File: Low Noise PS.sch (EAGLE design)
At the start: 64 parts, among them IC1 MAX6350SO08, IC2 OP27, IC3 LT1677, IC4 LT1677, IC5 MC79M12CDTG, IC6 MC78M12BDTG, Q1 MMBT2907AMMBTA56SOT23, Q2 MMBT5550SOT23, Q3 PMBF170, Q4 BSH201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

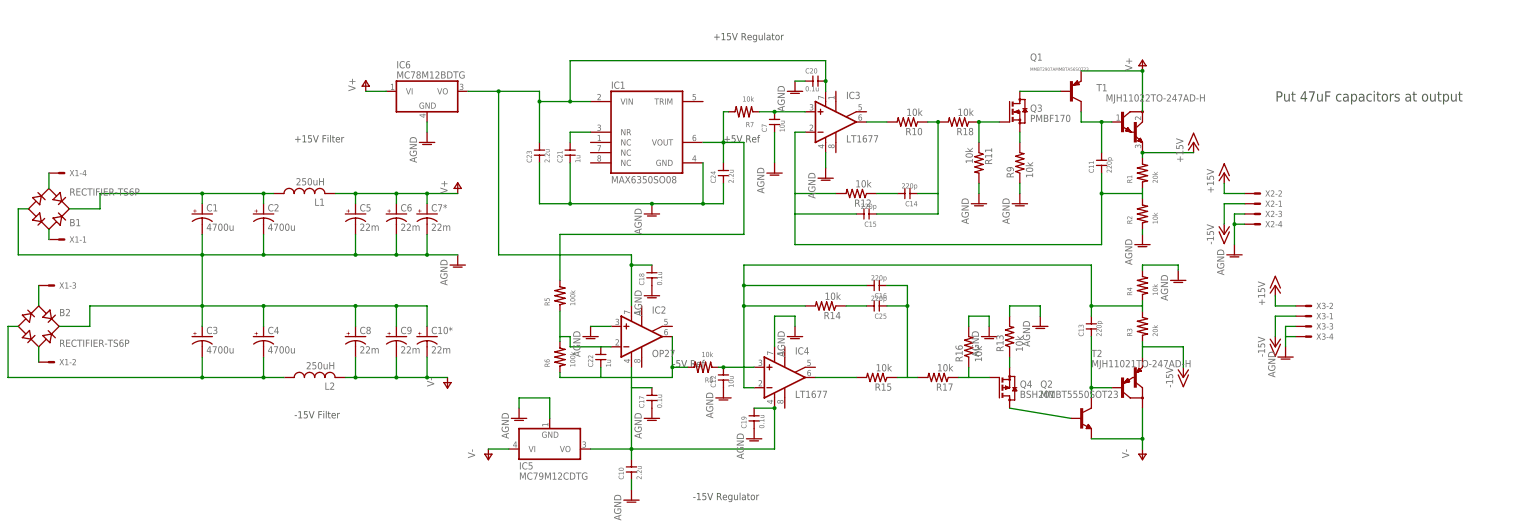
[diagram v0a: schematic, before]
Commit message: Almost ready to print
1) "cosmetic" adjustments needed (mainly increasing clearance for traces
below SMD parts)
2) component values need to be adjusted and chosen
3) Silkscreen needs to be cleaned
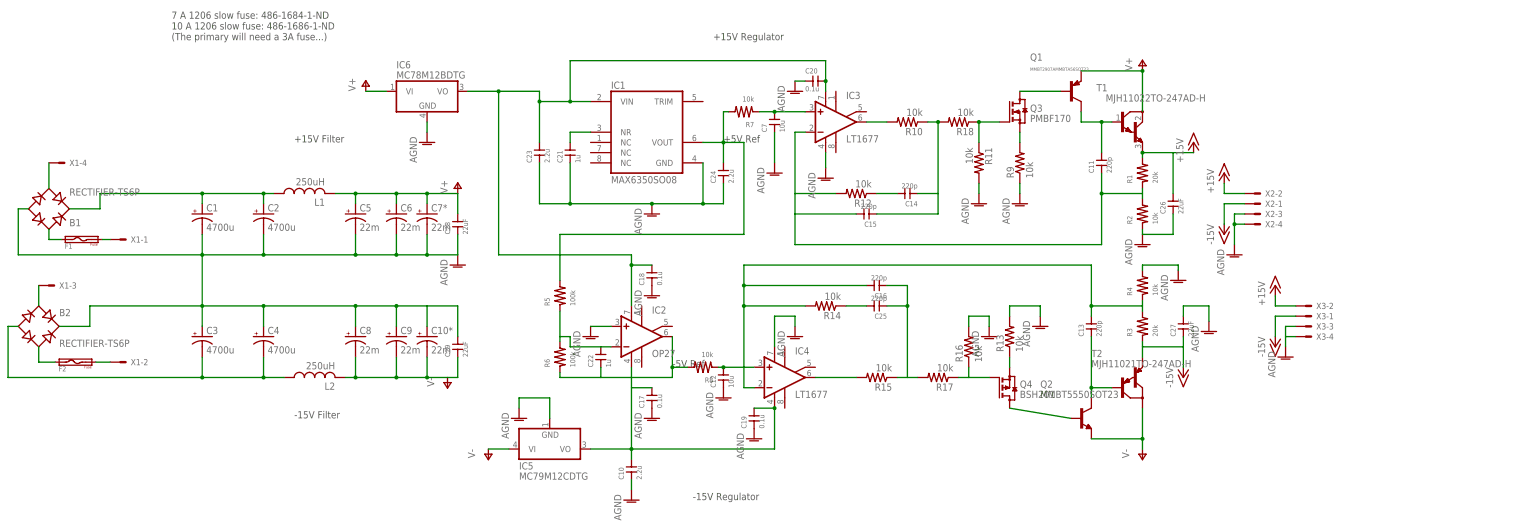
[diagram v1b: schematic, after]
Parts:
- added C26, C27, C28, C29: 22uF, rlc-jqi:CAP1206
- added F1, F2: (no value), jqi-power-supply:FUSE1206
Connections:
- new net N$22: F2.P$2, X1-2.S
- new net N$24: B2.AC2, F2.P$1
- net +15V: now also C26.P$2
- net -15V: now also C27.P$1
- net AGND: now also C26.P$1, C27.P$2, C28.P$1, C29.P$2
- net N$1: now also F1.P$1; no longer X1-1.S
- net N$5: now also F1.P$2, X1-1.S; no longer B2.AC2, X1-2.S
- net V+: now also C28.P$2
- net V-: now also C29.P$1
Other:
- note added: "7 A 1206 slow fuse: 486-1684-1-ND 10 A 1206 slow fuse: 486-1686-1-ND (The primary will need a 3A fuse...)"
- note removed: "Put 47uF capacitors at output"
- moved on the sheet: X1-1, X1-2, X1-4
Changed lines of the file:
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@@
 <part name="R17" library="rcl" deviceset="R-US_" device="R1206" value="10k"/>
 <part name="R18" library="rcl" deviceset="R-US_" device="R1206" value="10k"/>
+<part name="F1" library="jqi-power-supply" deviceset="FUSE" device="1206">
+<attribute name="DIGIKEY" value="486-1686-1-ND"/>
+</part>
+<part name="F2" library="jqi-power-supply" deviceset="FUSE" device="1206">
+<attribute name="DIGIKEY" value="486-1686-1-ND"/>
+</part>
+<part name="C26" library="rlc-jqi" deviceset="CAP" device="1206" value="22uF">
+<attribute name="DIGIKEY" value="445-8045-1-ND"/>
+</part>
+<part name="C27" library="rlc-jqi" deviceset="CAP" device="1206" value="22uF">
+<attribute name="DIGIKEY" value="445-8045-1-ND"/>
+</part>
+<part name="AGND23" library="supply1" deviceset="AGND" device=""/>
+<part name="C28" library="rlc-jqi" deviceset="CAP" device="1206" value="22uF">
+<attribute name="DIGIKEY" value="445-8045-1-ND"/>
+</part>
+<part name="C29" library="rlc-jqi" deviceset="CAP" device="1206" value="22uF">
+<attribute name="DIGIKEY" value="445-8045-1-ND"/>
+</part>
 </parts>
 <sheets>
@@
 <text x="190.5" y="2.54" size="1.778" layer="97">-15V Filter</text>
 <text x="190.5" y="71.12" size="1.778" layer="97">+15V Filter</text>
-<text x="434.34" y="81.28" size="2.54" layer="97">Put 47uF capacitors at output</text>
+<text x="160.02" y="96.52" size="1.778" layer="97">7 A 1206 slow fuse: 486-1684-1-ND
+10 A 1206 slow fuse: 486-1686-1-ND
+(The primary will need a 3A fuse...)</text>
 </plain>
 <instances>
-<instance part="X1" gate="-1" x="132.08" y="46.99"/>
-<instance part="X1" gate="-2" x="129.54" y="16.51"/>
+<instance part="X1" gate="-1" x="147.32" y="46.99"/>
+<instance part="X1" gate="-2" x="147.32" y="16.51"/>
 <instance part="X1" gate="-3" x="129.54" y="35.56"/>
-<instance part="X1" gate="-4" x="132.08" y="63.5"/>
+<instance part="X1" gate="-4" x="132.08" y="66.04"/>
 <instance part="B1" gate="G$1" x="129.54" y="54.61" rot="MR180"/>
 <instance part="B2" gate="G$1" x="127" y="25.4"/>
@@
 <instance part="R17" gate="G$1" x="350.52" y="12.7" rot="R180"/>
 <instance part="R18" gate="G$1" x="355.6" y="76.2" rot="R180"/>
+<instance part="F1" gate="G$1" x="137.668" y="46.99">
+<attribute name="DIGIKEY" x="137.668" y="46.99" size="1.778" layer="96" display="off"/>
+</instance>
+<instance part="F2" gate="G$1" x="136.144" y="16.51">
+<attribute name="DIGIKEY" x="136.144" y="16.51" size="1.778" layer="96" display="off"/>
+</instance>
+<instance part="C26" gate="G$1" x="408.94" y="55.88" rot="R90">
+<attribute name="DIGIKEY" x="408.94" y="55.88" size="1.778" layer="96" rot="R90" display="off"/>
+</instance>
+<instance part="C27" gate="G$1" x="411.48" y="25.4" rot="R90">
+<attribute name="DIGIKEY" x="411.48" y="25.4" size="1.778" layer="96" rot="R90" display="off"/>
+</instance>
+<instance part="AGND23" gate="VR1" x="417.83" y="24.13"/>
+<instance part="C28" gate="G$1" x="231.14" y="50.8" rot="R90">
+<attribute name="DIGIKEY" x="231.14" y="50.8" size="1.778" layer="96" rot="R90" display="off"/>
+</instance>
+<instance part="C29" gate="G$1" x="231.14" y="20.32" rot="R90">
+<attribute name="DIGIKEY" x="231.14" y="20.32" size="1.778" layer="96" rot="R90" display="off"/>
+</instance>
 </instances>
 <busses>
@@
 <wire x1="124.46" y1="54.61" x2="121.92" y2="54.61" width="0.1524" layer="91"/>
 <wire x1="121.92" y1="54.61" x2="121.92" y2="43.18" width="0.1524" layer="91"/>
+<pinref part="C29" gate="G$1" pin="P$2"/>
+<wire x1="223.52" y1="30.48" x2="231.14" y2="30.48" width="0.1524" layer="91"/>
+<wire x1="231.14" y1="30.48" x2="231.14" y2="22.86" width="0.1524" layer="91"/>
+<pinref part="C28" gate="G$1" pin="P$1"/>
+<wire x1="231.14" y1="43.18" x2="231.14" y2="48.26" width="0.1524" layer="91"/>
 </segment>
 <segment>
@@
 <pinref part="AGND14" gate="VR1" pin="AGND"/>
 <wire x1="401.32" y1="48.26" x2="401.32" y2="49.53" width="0.1524" layer="91"/>
+<pinref part="C26" gate="G$1" pin="P$1"/>
+<wire x1="401.32" y1="48.26" x2="408.94" y2="48.26" width="0.1524" layer="91"/>
+<wire x1="408.94" y1="48.26" x2="408.94" y2="53.34" width="0.1524" layer="91"/>
 </segment>
 <segment>
@@
 <wire x1="309.88" y1="73.66" x2="309.88" y2="66.04" width="0.1524" layer="91"/>
 <pinref part="AGND11" gate="VR1" pin="AGND"/>
+</segment>
+<segment>
+<pinref part="C27" gate="G$1" pin="P$2"/>
+<wire x1="411.48" y1="27.94" x2="411.48" y2="30.48" width="0.1524" layer="91"/>
+<pinref part="AGND23" gate="VR1" pin="AGND"/>
+<wire x1="411.48" y1="30.48" x2="417.83" y2="30.48" width="0.1524" layer="91"/>
+<wire x1="417.83" y1="30.48" x2="417.83" y2="26.67" width="0.1524" layer="91"/>
 </segment>
 </net>
@@
 <pinref part="P-1" gate="1" pin="V-"/>
 <wire x1="228.6" y1="12.7" x2="223.52" y2="12.7" width="0.1524" layer="91"/>
+<pinref part="C29" gate="G$1" pin="P$1"/>
+<wire x1="231.14" y1="17.78" x2="231.14" y2="12.7" width="0.1524" layer="91"/>
+<wire x1="231.14" y1="12.7" x2="228.6" y2="12.7" width="0.1524" layer="91"/>
 </segment>
 <segment>
@@
 <pinref part="P+1" gate="1" pin="V+"/>
 <junction x="223.52" y="58.42"/>
+<pinref part="C28" gate="G$1" pin="P$2"/>
+<wire x1="231.14" y1="53.34" x2="231.14" y2="58.42" width="0.1524" layer="91"/>
 </segment>
 <segment>
@@
 <wire x1="401.32" y1="20.32" x2="411.48" y2="20.32" width="0.1524" layer="91"/>
 <wire x1="411.48" y1="20.32" x2="411.48" y2="15.24" width="0.1524" layer="91"/>
+<pinref part="C27" gate="G$1" pin="P$1"/>
+<wire x1="411.48" y1="20.32" x2="411.48" y2="22.86" width="0.1524" layer="91"/>
 </segment>
 <segment>
@@
 <pinref part="P+4" gate="1" pin="+15V"/>
 <pinref part="T1" gate="G$1" pin="E"/>
-<wire x1="414.02" y1="68.58" x2="401.32" y2="68.58" width="0.1524" layer="91"/>
+<wire x1="414.02" y1="68.58" x2="408.94" y2="68.58" width="0.1524" layer="91"/>
+<wire x1="408.94" y1="68.58" x2="401.32" y2="68.58" width="0.1524" layer="91"/>
 <wire x1="401.32" y1="68.58" x2="401.32" y2="67.31" width="0.1524" layer="91"/>
 <pinref part="R1" gate="G$1" pin="P$2"/>
 <junction x="401.32" y="68.58"/>
+<pinref part="C26" gate="G$1" pin="P$2"/>
+<wire x1="408.94" y1="58.42" x2="408.94" y2="68.58" width="0.1524" layer="91"/>
 </segment>
 <segment>
@@
 </segment>
 </net>
-<net name="N$1" class="0">
-<segment>
-<pinref part="X1" gate="-1" pin="S"/>
-<pinref part="B1" gate="G$1" pin="AC1"/>
-<wire x1="129.54" y1="46.99" x2="129.54" y2="49.53" width="0.1524" layer="91"/>
-</segment>
-</net>
 <net name="N$2" class="0">
 <segment>
 <pinref part="X1" gate="-4" pin="S"/>
 <pinref part="B1" gate="G$1" pin="AC2"/>
-<wire x1="129.54" y1="63.5" x2="129.54" y2="59.69" width="0.1524" layer="91"/>
-</segment>
-</net>
-<net name="N$5" class="0">
-<segment>
-<pinref part="B2" gate="G$1" pin="AC2"/>
-<pinref part="X1" gate="-2" pin="S"/>
-<wire x1="127" y1="20.32" x2="127" y2="16.51" width="0.1524" layer="91"/>
+<wire x1="129.54" y1="66.04" x2="129.54" y2="59.69" width="0.1524" layer="91"/>
 </segment>
 </net>
@@
 </segment>
 </net>
+<net name="N$1" class="0">
+<segment>
+<pinref part="B1" gate="G$1" pin="AC1"/>
+<wire x1="129.54" y1="49.53" x2="129.54" y2="46.99" width="0.1524" layer="91"/>
+<pinref part="F1" gate="G$1" pin="P$1"/>
+<wire x1="129.54" y1="46.99" x2="132.588" y2="46.99" width="0.1524" layer="91"/>
+</segment>
+</net>
+<net name="N$5" class="0">
+<segment>
+<pinref part="F1" gate="G$1" pin="P$2"/>
+<pinref part="X1" gate="-1" pin="S"/>
+<wire x1="142.748" y1="46.99" x2="144.78" y2="46.99" width="0.1524" layer="91"/>
+</segment>
+</net>
+<net name="N$22" class="0">
+<segment>
+<pinref part="F2" gate="G$1" pin="P$2"/>
+<pinref part="X1" gate="-2" pin="S"/>
+<wire x1="141.224" y1="16.51" x2="144.78" y2="16.51" width="0.1524" layer="91"/>
+</segment>
+</net>
+<net name="N$24" class="0">
+<segment>
+<pinref part="F2" gate="G$1" pin="P$1"/>
+<pinref part="B2" gate="G$1" pin="AC2"/>
+<wire x1="131.064" y1="16.51" x2="127" y2="16.51" width="0.1524" layer="91"/>
+<wire x1="127" y1="16.51" x2="127" y2="20.32" width="0.1524" layer="91"/>
+</segment>
+</net>
 </nets>
 </sheet>
@@
 </schematic>
 </drawing>
+<compatibility>
+<note version="6.3" minversion="6.2.2" severity="warning">
+Since Version 6.2.2 text objects can contain more than one line,
+which will not be processed correctly with this version.
+</note>
+</compatibility>
 </eagle>

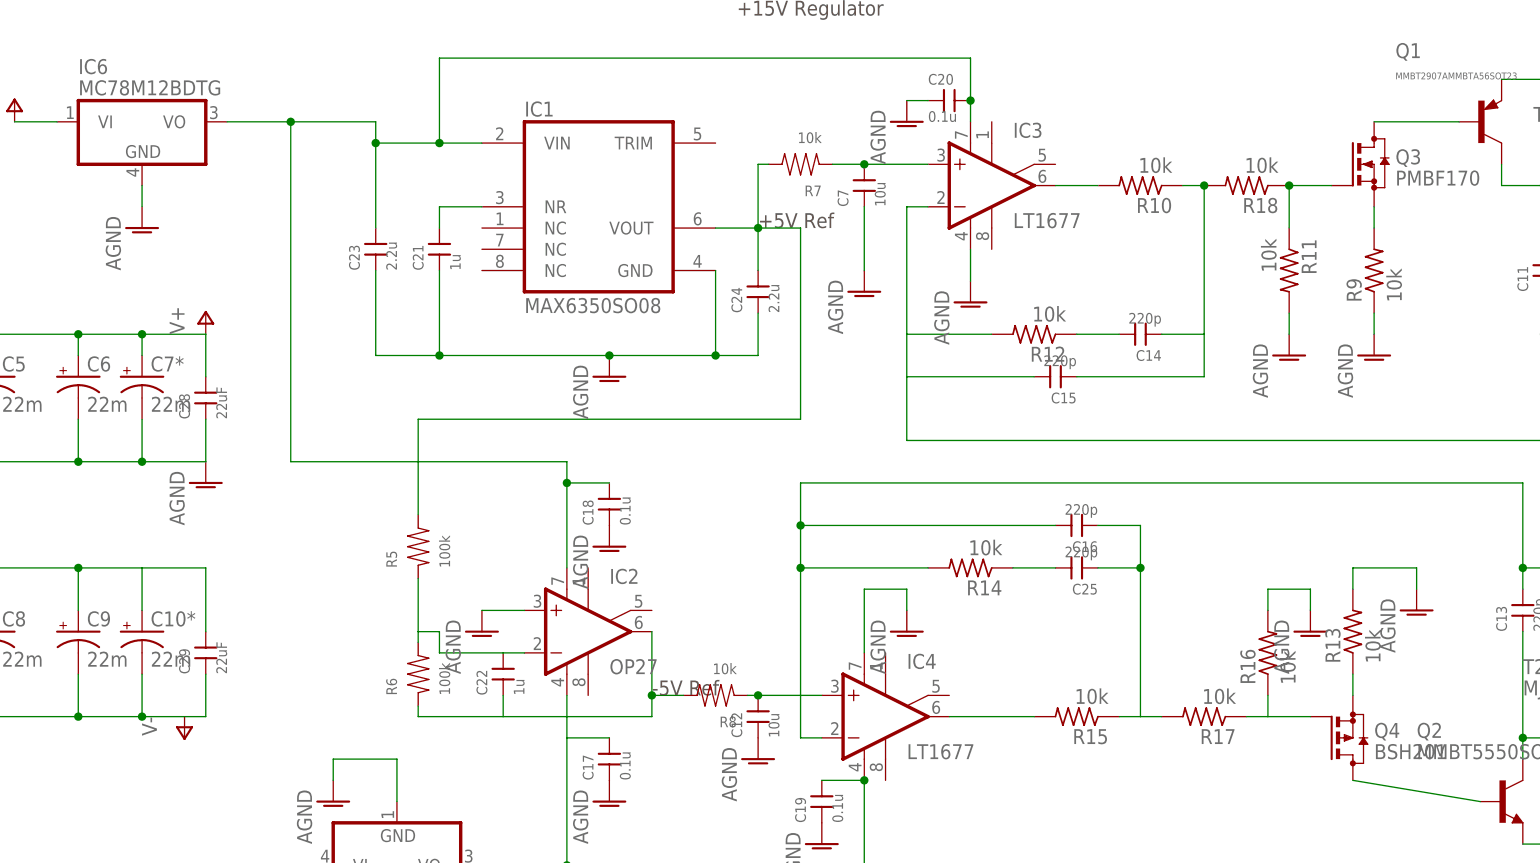
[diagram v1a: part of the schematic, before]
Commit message: BOM and part attributes adjusted
This commit is not quite the final one:  a performance test must be done
before putting it into production. Also it might be useful to reorder
part names to make assembly easy.
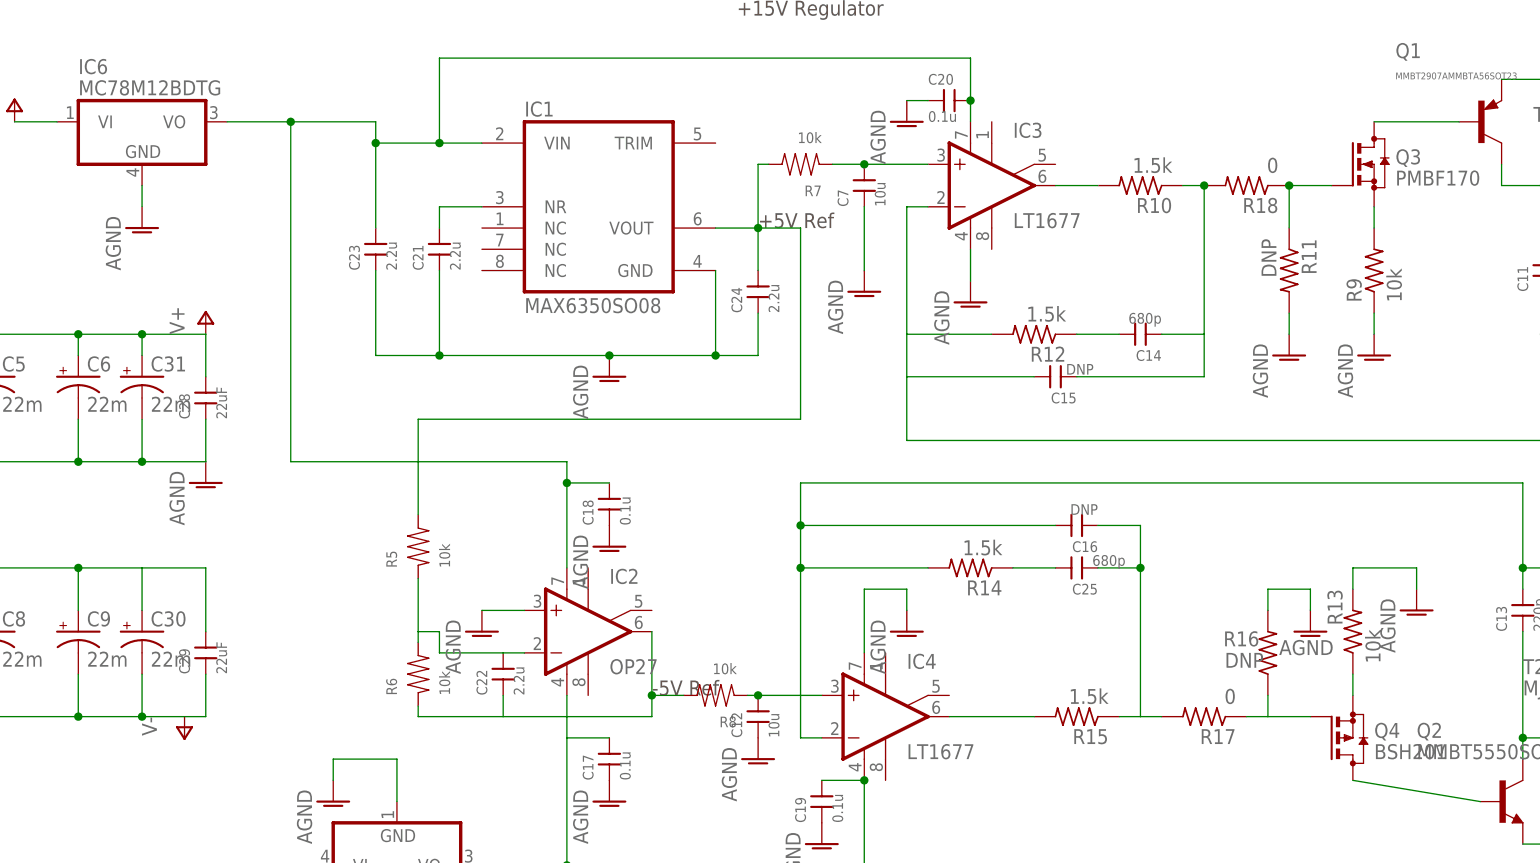
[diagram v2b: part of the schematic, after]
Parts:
- C10, C23, C24: DIGIKEY (none) -> 587-2402-1-ND
- C11, C13: DIGIKEY (none) -> 1276-1166-1-ND
- C14, C25: value 220p -> 680p; DIGIKEY (none) -> 399-8209-1-ND
- C15, C16: value 220p -> DNP
- C17, C18, C19, C20: DIGIKEY (none) -> 399-1249-1-ND
- C21, C22: value 1u -> 2.2u; DIGIKEY (none) -> 587-2402-1-ND
- IC2: DIGIKEY (none) -> OP27GSZ-REEL7CT-ND
- IC3, IC4: DIGIKEY (none) -> LT1677CS8#PBF-ND
- Q2: DIGIKEY (none) -> MMBT5550CT-ND
- Q3: DIGIKEY (none) -> MMBT2907AFSCT-ND
- Q4: DIGIKEY (none) -> 568-6217-1-ND
- R1, R3: DIGIKEY (none) -> RMCF1206FT20K0CT-ND
- R10, R12, R14, R15: value 10k -> 1.5k; DIGIKEY (none) -> 541-1.5KECT-ND
- R11, R16: value 10k -> DNP
- R13, R2, R4, R7, R8, R9: DIGIKEY (none) -> RNCP1206FTD10K0CT-ND
- R17, R18: value 10k -> 0; DIGIKEY (none) -> RMCF1206ZT0R00CT-ND
- R5, R6: value 100k -> 10k; DIGIKEY (none) -> RNCP1206FTD10K0CT-ND
- renumbered C10* to C30, C7* to C31
